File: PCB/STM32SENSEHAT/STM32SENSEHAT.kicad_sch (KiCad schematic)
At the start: 0 parts

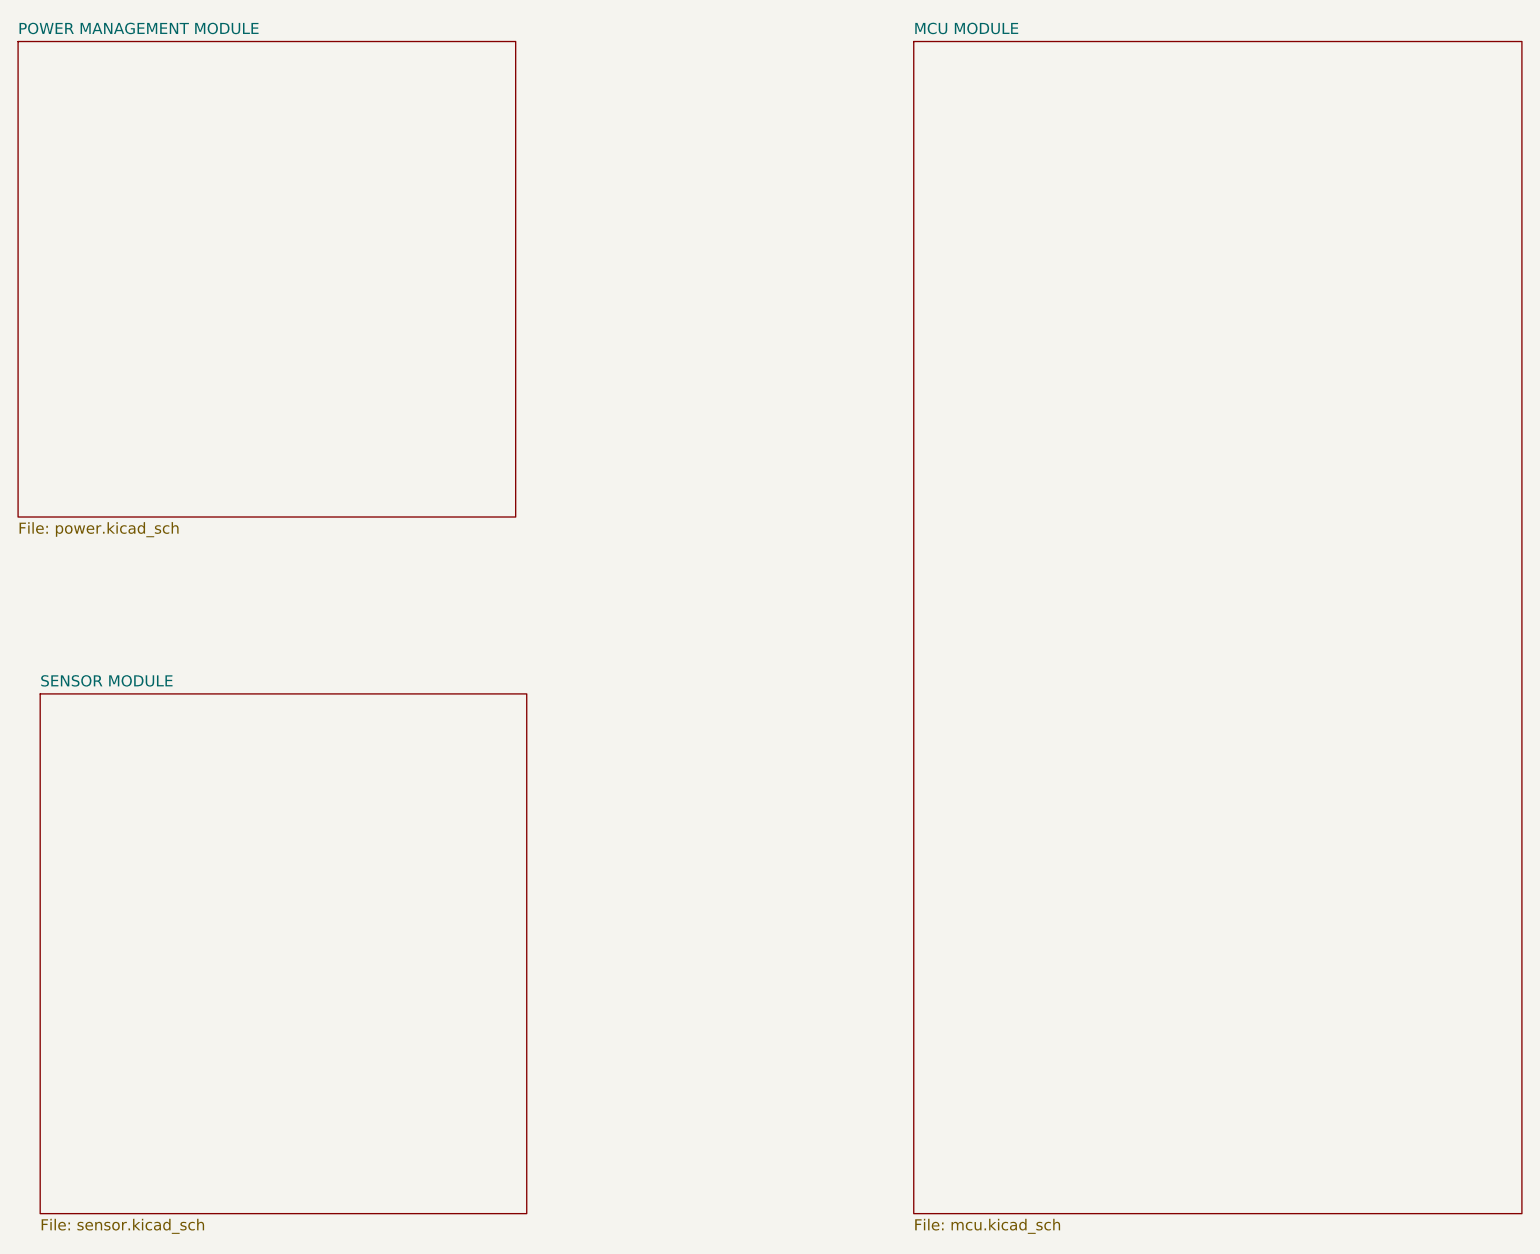
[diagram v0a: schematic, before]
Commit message: rework of top level sheet, MCU, power and sensor sheet
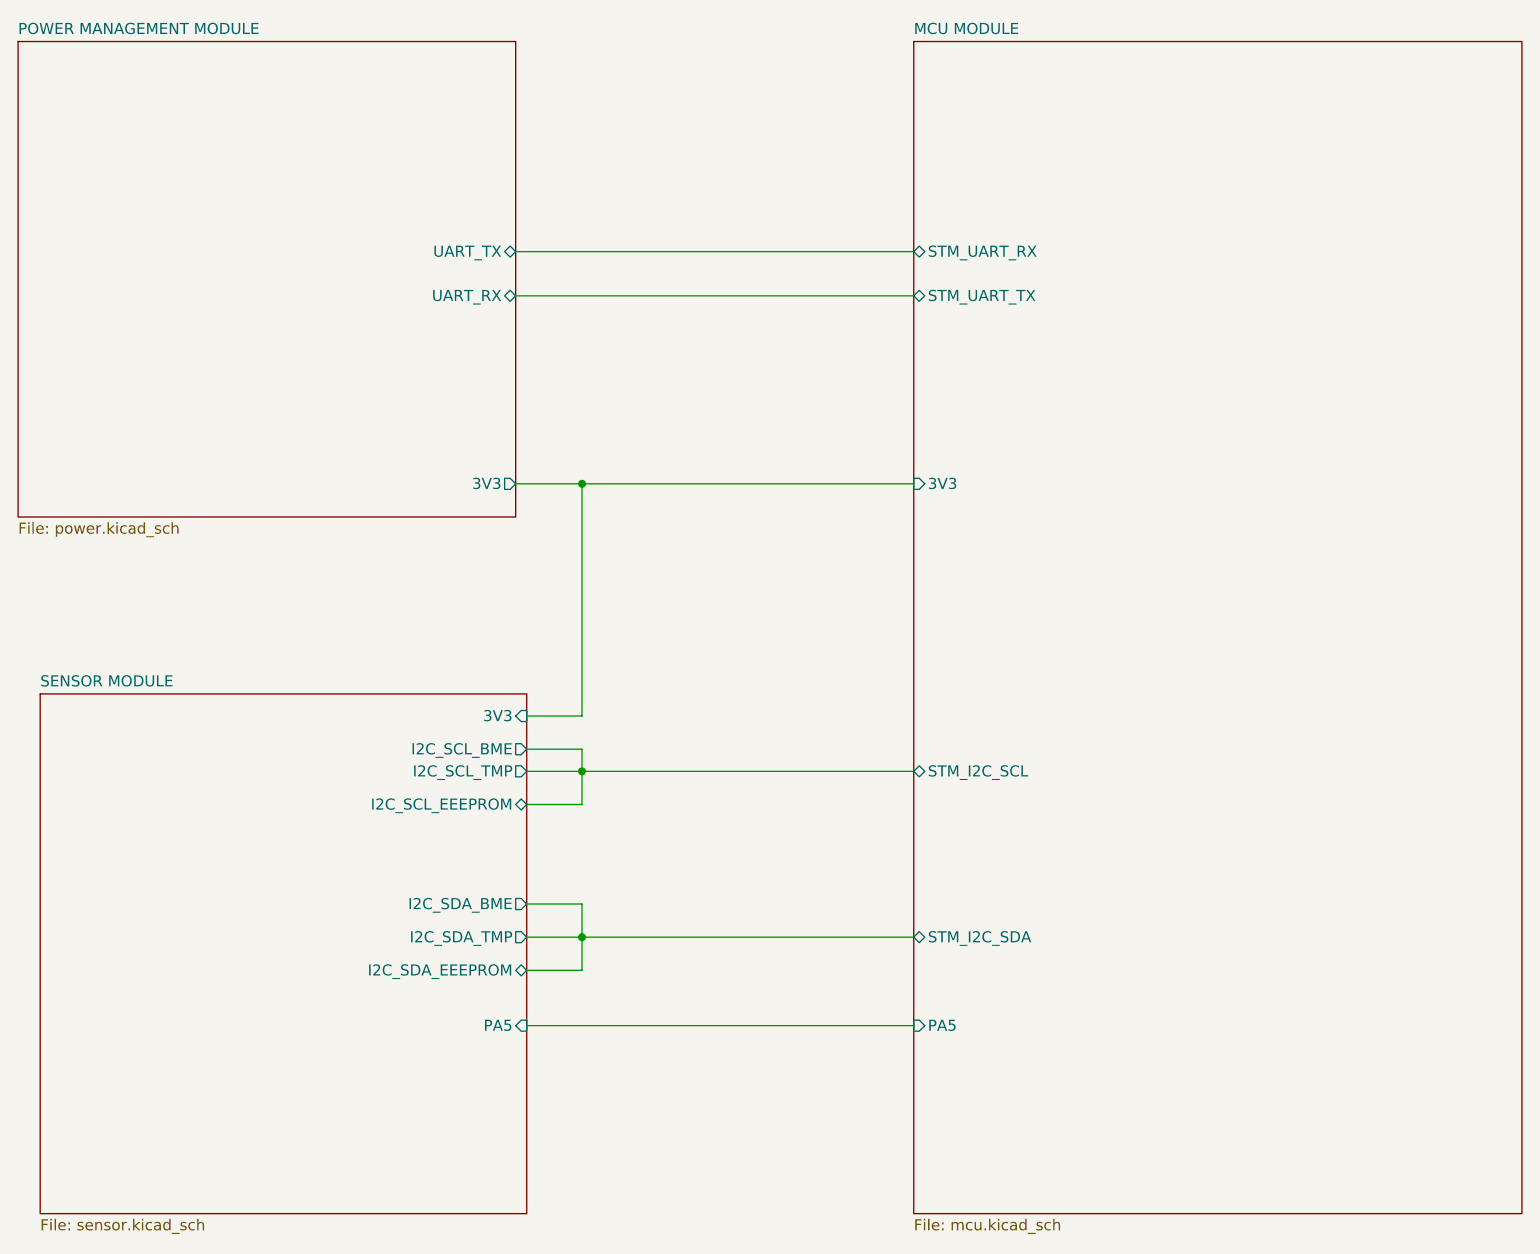
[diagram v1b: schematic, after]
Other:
- sheet MCU MODULE ports: added 3V3, PA5, STM_I2C_SCL, STM_I2C_SDA, STM_UART_RX, STM_UART_TX; removed none
- sheet POWER MANAGEMENT MODULE ports: added 3V3, UART_RX, UART_TX; removed none
- sheet SENSOR MODULE ports: added 3V3, I2C_SCL_BME, I2C_SCL_EEEPROM, I2C_SCL_TMP, I2C_SDA_BME, I2C_SDA_EEEPROM, I2C_SDA_TMP, PA5; removed none
- company: (none) -> IMPERIUM
- title: (none) -> STM32-ENVIRO-SENSING-TOP-LEVEL
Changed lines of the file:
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@@
 (kicad_sch (version 20230121) (generator eeschema)
   (paper "A4")
+  (title_block
+    (title "STM32-ENVIRO-SENSING-TOP-LEVEL")
+    (date "2023-03-04")
+    (rev "V0.0")
+    (company "IMPERIUM")
+    (comment 1 "TRAVIMADOX WEBB")
+    (comment 2 "PHOMOLO MAKINA")
+    (comment 3 "RUMBIDZAI MASHUMBA")
+    (comment 4 "AUTHOR(S)")
+  )
+  (junction (at 99.06 73.66) (diameter 0) (color 0 0 0 0)
+  )
+  (junction (at 99.06 125.73) (diameter 0) (color 0 0 0 0)
+  )
+  (junction (at 99.06 106.68) (diameter 0) (color 0 0 0 0)
+  )
+  (wire (pts (xy 91.44 46.99) (xy 137.16 46.99))
+    (stroke (width 0) (type default))
+  )
+  (wire (pts (xy 99.06 106.68) (xy 137.16 106.68))
+    (stroke (width 0) (type default))
+  )
+  (wire (pts (xy 91.44 73.66) (xy 99.06 73.66))
+    (stroke (width 0) (type default))
+  )
+  (wire (pts (xy 99.06 73.66) (xy 137.16 73.66))
+    (stroke (width 0) (type default))
+  )
+  (wire (pts (xy 99.06 121.92) (xy 99.06 125.73))
+    (stroke (width 0) (type default))
+  )
+  (wire (pts (xy 92.71 121.92) (xy 99.06 121.92))
+    (stroke (width 0) (type default))
+  )
+  (wire (pts (xy 92.71 106.68) (xy 99.06 106.68))
+    (stroke (width 0) (type default))
+  )
+  (wire (pts (xy 92.71 125.73) (xy 99.06 125.73))
+    (stroke (width 0) (type default))
+  )
+  (wire (pts (xy 91.44 52.07) (xy 137.16 52.07))
+    (stroke (width 0) (type default))
+  )
+  (wire (pts (xy 99.06 106.68) (xy 99.06 110.49))
+    (stroke (width 0) (type default))
+  )
+  (wire (pts (xy 92.71 100.33) (xy 99.06 100.33))
+    (stroke (width 0) (type default))
+  )
+  (wire (pts (xy 99.06 100.33) (xy 99.06 73.66))
+    (stroke (width 0) (type default))
+  )
+  (wire (pts (xy 99.06 125.73) (xy 99.06 129.54))
+    (stroke (width 0) (type default))
+  )
+  (wire (pts (xy 99.06 129.54) (xy 92.71 129.54))
+    (stroke (width 0) (type default))
+  )
+  (wire (pts (xy 92.71 135.89) (xy 137.16 135.89))
+    (stroke (width 0) (type default))
+  )
+  (wire (pts (xy 92.71 104.14) (xy 99.06 104.14))
+    (stroke (width 0) (type default))
+  )
+  (wire (pts (xy 92.71 110.49) (xy 99.06 110.49))
+    (stroke (width 0) (type default))
+  )
+  (wire (pts (xy 99.06 104.14) (xy 99.06 106.68))
+    (stroke (width 0) (type default))
+  )
+  (wire (pts (xy 99.06 125.73) (xy 137.16 125.73))
+    (stroke (width 0) (type default))
+  )
   (sheet (at 36.83 97.79) (size 55.88 59.69) (fields_autoplaced)
     (stroke (width 0.1524) (type solid))
-    (fill (color 0 255 0 1.0000))
+    (fill (color 255 255 255 1.0000))
     (property "Sheetname" "SENSOR MODULE" (at 36.83 97.0784 0)
       (effects (font (size 1.27 1.27)) (justify left bottom))
@@
     (property "Sheetfile" "sensor.kicad_sch" (at 36.83 158.0646 0)
       (effects (font (size 1.27 1.27)) (justify left top))
+    )
+    (pin "PA5" input (at 92.71 135.89 0)
+      (effects (font (size 1.27 1.27)) (justify right))
+    )
+    (pin "I2C_SDA_BME" output (at 92.71 121.92 0)
+      (effects (font (size 1.27 1.27)) (justify right))
+    )
+    (pin "I2C_SCL_BME" output (at 92.71 104.14 0)
+      (effects (font (size 1.27 1.27)) (justify right))
+    )
+    (pin "I2C_SCL_TMP" output (at 92.71 106.68 0)
+      (effects (font (size 1.27 1.27)) (justify right))
+    )
+    (pin "I2C_SCL_EEEPROM" bidirectional (at 92.71 110.49 0)
+      (effects (font (size 1.27 1.27)) (justify right))
+    )
+    (pin "I2C_SDA_TMP" output (at 92.71 125.73 0)
+      (effects (font (size 1.27 1.27)) (justify right))
+    )
+    (pin "I2C_SDA_EEEPROM" bidirectional (at 92.71 129.54 0)
+      (effects (font (size 1.27 1.27)) (justify right))
+    )
+    (pin "3V3" input (at 92.71 100.33 0)
+      (effects (font (size 1.27 1.27)) (justify right))
     )
     (instances
@@
   (sheet (at 137.16 22.86) (size 69.85 134.62) (fields_autoplaced)
     (stroke (width 0.1524) (type solid))
-    (fill (color 0 255 0 1.0000))
+    (fill (color 255 255 255 1.0000))
     (property "Sheetname" "MCU MODULE" (at 137.16 22.1484 0)
       (effects (font (size 1.27 1.27)) (justify left bottom))
@@
     (property "Sheetfile" "mcu.kicad_sch" (at 137.16 158.0646 0)
       (effects (font (size 1.27 1.27)) (justify left top))
+    )
+    (pin "STM_UART_RX" bidirectional (at 137.16 46.99 180)
+      (effects (font (size 1.27 1.27)) (justify left))
+    )
+    (pin "STM_UART_TX" bidirectional (at 137.16 52.07 180)
+      (effects (font (size 1.27 1.27)) (justify left))
+    )
+    (pin "STM_I2C_SCL" bidirectional (at 137.16 106.68 180)
+      (effects (font (size 1.27 1.27)) (justify left))
+    )
+    (pin "STM_I2C_SDA" bidirectional (at 137.16 125.73 180)
+      (effects (font (size 1.27 1.27)) (justify left))
+    )
+    (pin "PA5" input (at 137.16 135.89 180)
+      (effects (font (size 1.27 1.27)) (justify left))
+    )
+    (pin "3V3" input (at 137.16 73.66 180)
+      (effects (font (size 1.27 1.27)) (justify left))
     )
     (instances
@@
   (sheet (at 34.29 22.86) (size 57.15 54.61) (fields_autoplaced)
     (stroke (width 0.1524) (type solid))
-    (fill (color 0 255 0 1.0000))
+    (fill (color 255 255 255 1.0000))
     (property "Sheetname" "POWER MANAGEMENT MODULE" (at 34.29 22.1484 0)
       (effects (font (size 1.27 1.27)) (justify left bottom))
@@
       (effects (font (size 1.27 1.27)) (justify left top))
     )
+    (pin "UART_RX" bidirectional (at 91.44 52.07 0)
+      (effects (font (size 1.27 1.27)) (justify right))
+    )
+    (pin "UART_TX" bidirectional (at 91.44 46.99 0)
+      (effects (font (size 1.27 1.27)) (justify right))
+    )
+    (pin "3V3" output (at 91.44 73.66 0)
+      (effects (font (size 1.27 1.27)) (justify right))
+    )
     (instances
